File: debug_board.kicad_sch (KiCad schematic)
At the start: 0 parts

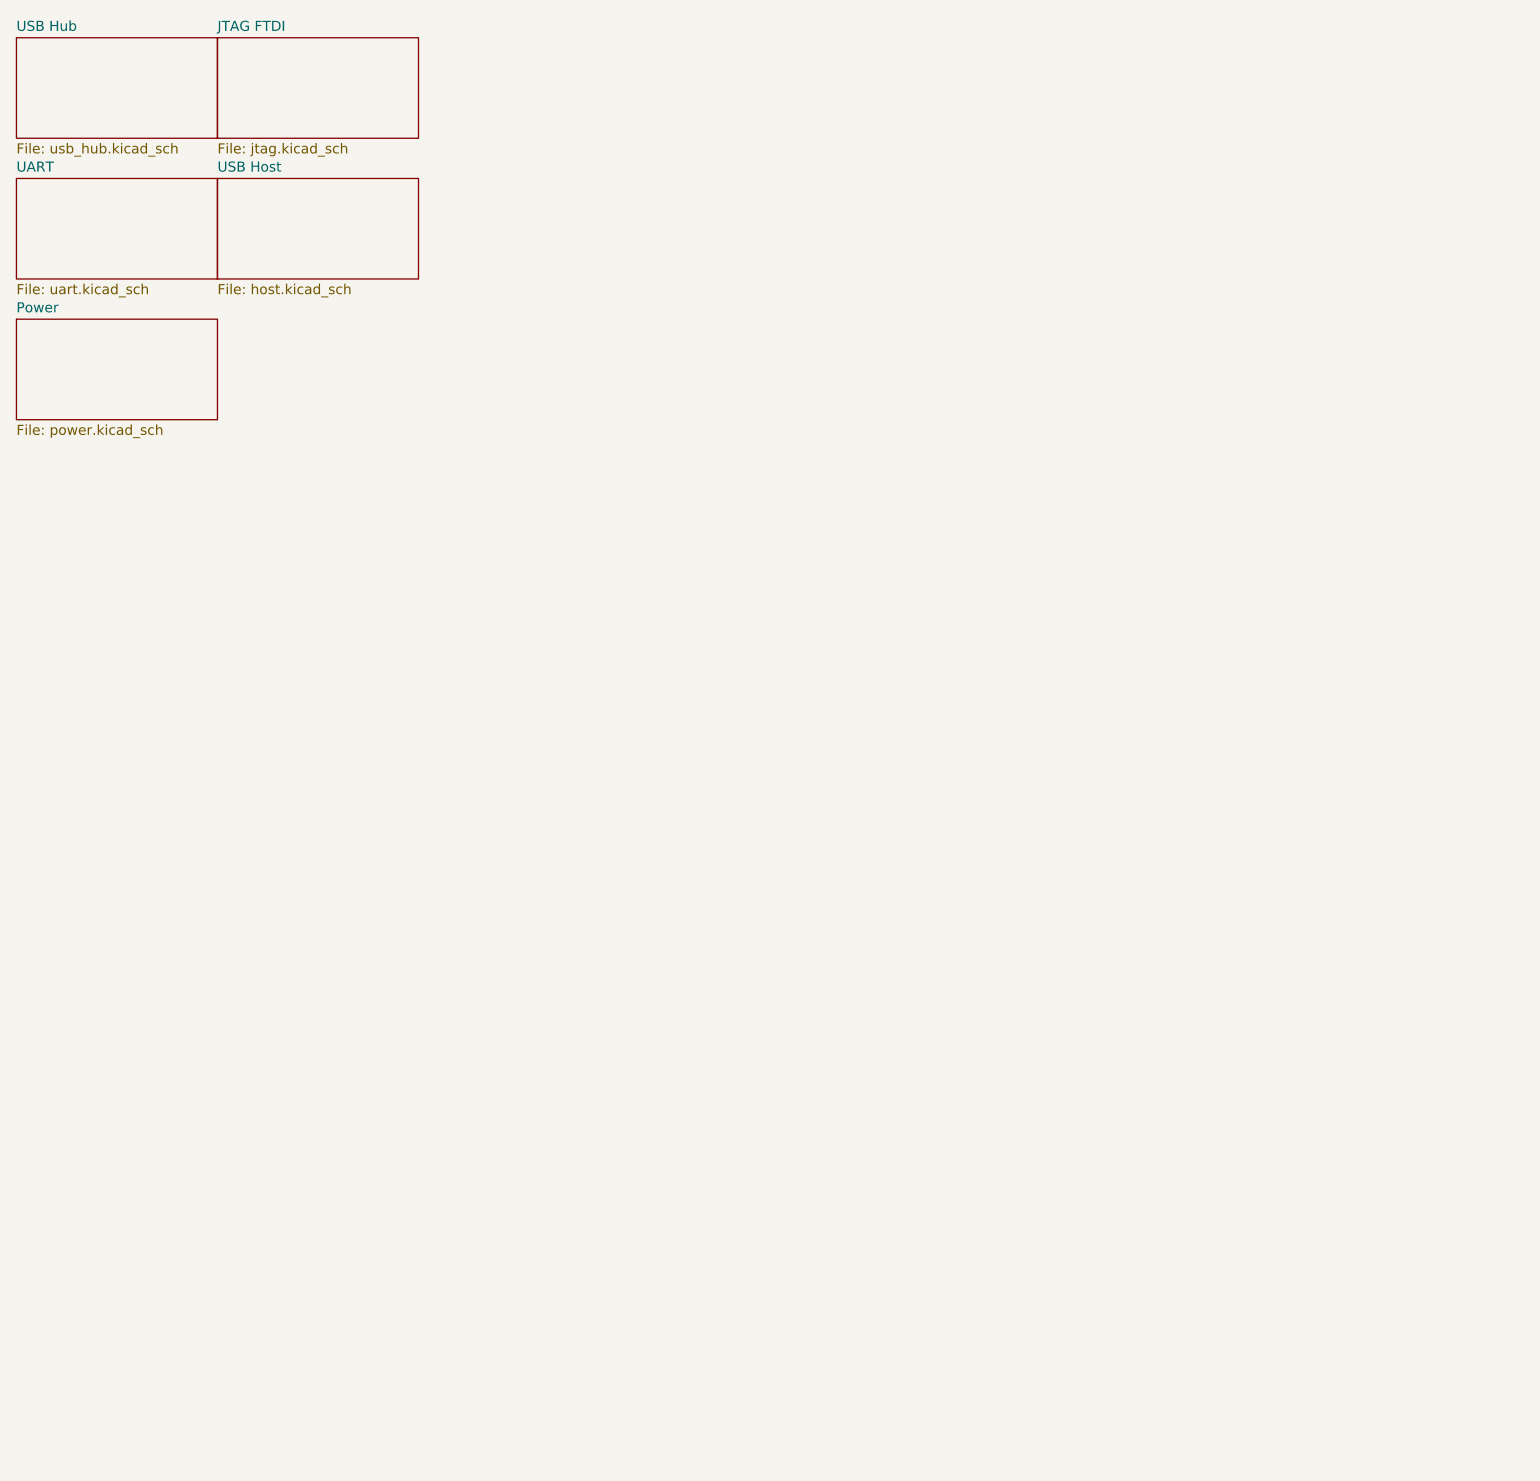
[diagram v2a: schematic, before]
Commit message: Used steppenprobe as base for our UART and JTAG.
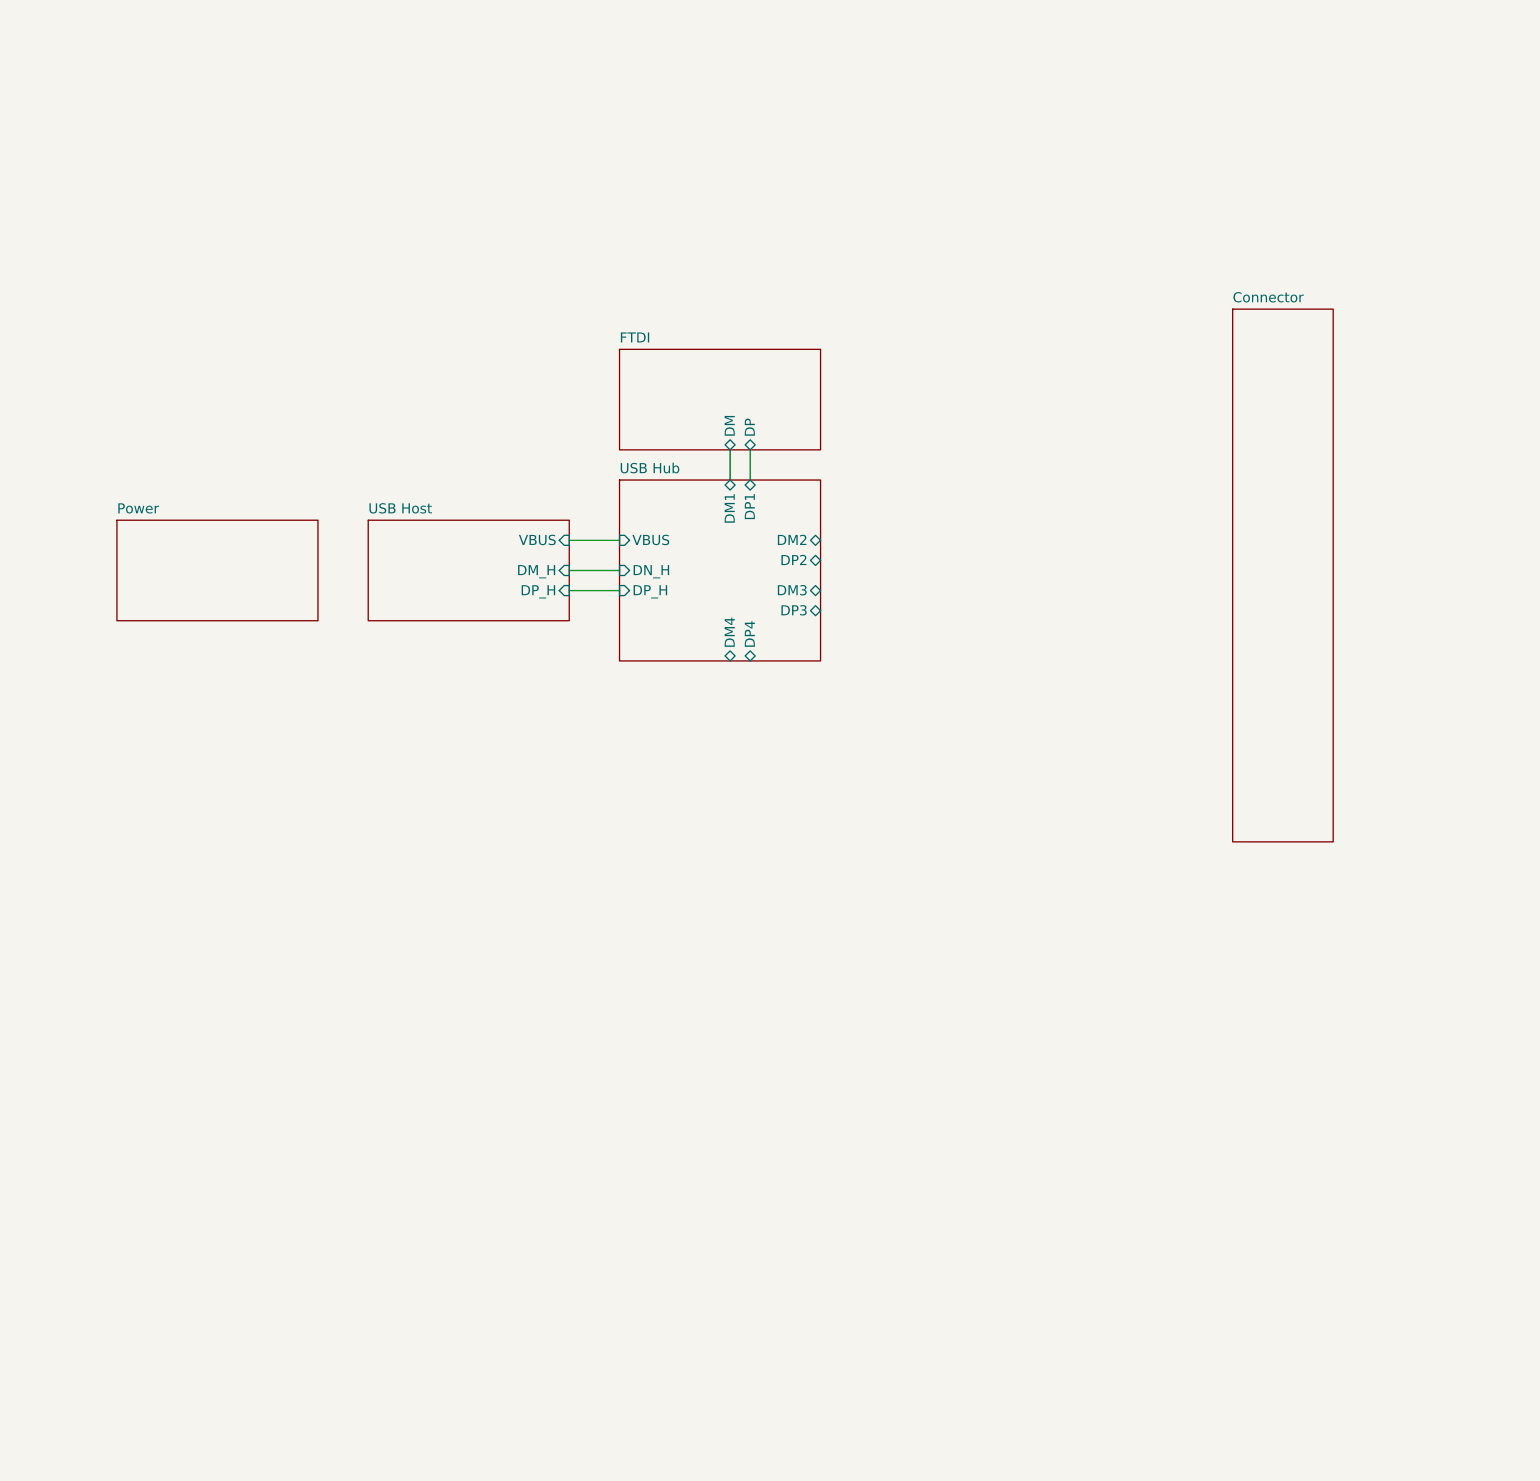
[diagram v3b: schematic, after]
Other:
- sheet JTAG FTDI renamed FTDI
- removed sheet UART
- added sheet Connector (connector.kicad_sch)
- sheet FTDI ports: added DM, DP; removed none
- sheet USB Host ports: added DM_H, DP_H, VBUS; removed none
- sheet USB Hub ports: added DM1, DM2, DM3, DM4, DN_H, DP1, DP2, DP3, DP4, DP_H, VBUS; removed none
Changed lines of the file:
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@@
 	(generator_version "8.0")
 	(paper "A4")
-	(sheet
-		(at 38.1 33.02)
+	(wire
+		(pts
+			(xy 82.55 82.55) (xy 88.9 82.55)
+		)
+		(stroke
+			(width 0)
+			(type default)
+		)
+	)
+	(wire
+		(pts
+			(xy 102.87 67.31) (xy 102.87 71.12)
+		)
+		(stroke
+			(width 0)
+			(type default)
+		)
+	)
+	(wire
+		(pts
+			(xy 105.41 67.31) (xy 105.41 71.12)
+		)
+		(stroke
+			(width 0)
+			(type default)
+		)
+	)
+	(wire
+		(pts
+			(xy 82.55 78.74) (xy 88.9 78.74)
+		)
+		(stroke
+			(width 0)
+			(type default)
+		)
+	)
+	(wire
+		(pts
+			(xy 82.55 85.09) (xy 88.9 85.09)
+		)
+		(stroke
+			(width 0)
+			(type default)
+		)
+	)
+	(sheet
+		(at 57.15 76.2)
 		(size 25.4 12.7)
 		(fields_autoplaced yes)
@@
 		)
 		(property "Sheetname" "USB Host"
-			(at 38.1 32.3084 0)
+			(at 57.15 75.4884 0)
 			(effects
 				(font
@@
 		)
 		(property "Sheetfile" "host.kicad_sch"
-			(at 38.1 46.3046 0)
-			(effects
-				(font
-					(size 1.27 1.27)
-				)
-				(justify left top)
+			(at 57.15 89.4846 0)
+			(effects
+				(font
+					(size 1.27 1.27)
+				)
+				(justify left top)
+				(hide yes)
+			)
+		)
+		(pin "VBUS" input
+			(at 82.55 78.74 0)
+			(effects
+				(font
+					(size 1.27 1.27)
+				)
+				(justify right)
+			)
+		)
+		(pin "DM_H" input
+			(at 82.55 82.55 0)
+			(effects
+				(font
+					(size 1.27 1.27)
+				)
+				(justify right)
+			)
+		)
+		(pin "DP_H" input
+			(at 82.55 85.09 0)
+			(effects
+				(font
+					(size 1.27 1.27)
+				)
+				(justify right)
 			)
 		)
@@
 	)
 	(sheet
-		(at 12.7 50.8)
+		(at 25.4 76.2)
 		(size 25.4 12.7)
 		(fields_autoplaced yes)
@@
 		)
 		(property "Sheetname" "Power"
-			(at 12.7 50.0884 0)
+			(at 25.4 75.4884 0)
 			(effects
 				(font
@@
 		)
 		(property "Sheetfile" "power.kicad_sch"
-			(at 12.7 64.0846 0)
-			(effects
-				(font
-					(size 1.27 1.27)
-				)
-				(justify left top)
+			(at 25.4 89.4846 0)
+			(effects
+				(font
+					(size 1.27 1.27)
+				)
+				(justify left top)
+				(hide yes)
 			)
 		)
@@
 	)
 	(sheet
-		(at 38.1 15.24)
+		(at 88.9 54.61)
 		(size 25.4 12.7)
 		(fields_autoplaced yes)
@@
 			(color 0 0 0 0.0000)
 		)
-		(property "Sheetname" "JTAG FTDI"
-			(at 38.1 14.5284 0)
+		(property "Sheetname" "FTDI"
+			(at 88.9 53.8984 0)
 			(effects
 				(font
@@
 		)
 		(property "Sheetfile" "jtag.kicad_sch"
-			(at 38.1 28.5246 0)
-			(effects
-				(font
-					(size 1.27 1.27)
-				)
-				(justify left top)
+			(at 88.9 67.8946 0)
+			(effects
+				(font
+					(size 1.27 1.27)
+				)
+				(justify left top)
+				(hide yes)
+			)
+		)
+		(pin "DM" bidirectional
+			(at 102.87 67.31 270)
+			(effects
+				(font
+					(size 1.27 1.27)
+				)
+				(justify left)
+			)
+		)
+		(pin "DP" bidirectional
+			(at 105.41 67.31 270)
+			(effects
+				(font
+					(size 1.27 1.27)
+				)
+				(justify left)
 			)
 		)
@@
 	)
 	(sheet
-		(at 12.7 33.02)
-		(size 25.4 12.7)
+		(at 88.9 71.12)
+		(size 25.4 22.86)
+		(stroke
+			(width 0.1524)
+			(type solid)
+		)
+		(fill
+			(color 0 0 0 0.0000)
+		)
+		(property "Sheetname" "USB Hub"
+			(at 88.9 70.4084 0)
+			(effects
+				(font
+					(size 1.27 1.27)
+				)
+				(justify left bottom)
+			)
+		)
+		(property "Sheetfile" "usb_hub.kicad_sch"
+			(at 98.044 69.088 0)
+			(effects
+				(font
+					(size 1.27 1.27)
+				)
+				(justify left top)
+				(hide yes)
+			)
+		)
+		(pin "DM2" bidirectional
+			(at 114.3 78.74 0)
+			(effects
+				(font
+					(size 1.27 1.27)
+				)
+				(justify right)
+			)
+		)
+		(pin "DM1" bidirectional
+			(at 102.87 71.12 90)
+			(effects
+				(font
+					(size 1.27 1.27)
+				)
+				(justify right)
+			)
+		)
+		(pin "DP1" bidirectional
+			(at 105.41 71.12 90)
+			(effects
+				(font
+					(size 1.27 1.27)
+				)
+				(justify right)
+			)
+		)
+		(pin "DP2" bidirectional
+			(at 114.3 81.28 0)
+			(effects
+				(font
+					(size 1.27 1.27)
+				)
+				(justify right)
+			)
+		)
+		(pin "DP3" bidirectional
+			(at 114.3 87.63 0)
+			(effects
+				(font
+					(size 1.27 1.27)
+				)
+				(justify right)
+			)
+		)
+		(pin "DM4" bidirectional
+			(at 102.87 93.98 270)
+			(effects
+				(font
+					(size 1.27 1.27)
+				)
+				(justify left)
+			)
+		)
+		(pin "DM3" bidirectional
+			(at 114.3 85.09 0)
+			(effects
+				(font
+					(size 1.27 1.27)
+				)
+				(justify right)
+			)
+		)
+		(pin "DP4" bidirectional
+			(at 105.41 93.98 270)
+			(effects
+				(font
+					(size 1.27 1.27)
+				)
+				(justify left)
+			)
+		)
+		(pin "VBUS" input
+			(at 88.9 78.74 180)
+			(effects
+				(font
+					(size 1.27 1.27)
+				)
+				(justify left)
+			)
+		)
+		(pin "DP_H" input
+			(at 88.9 85.09 180)
+			(effects
+				(font
+					(size 1.27 1.27)
+				)
+				(justify left)
+			)
+		)
+		(pin "DN_H" input
+			(at 88.9 82.55 180)
+			(effects
+				(font
+					(size 1.27 1.27)
+				)
+				(justify left)
+			)
+		)
+		(instances
+			(project "debug_board"
+				(path "/9ba02813-5189-4482-9c9e-35a29bc7aded"
+					(page "3")
+				)
+			)
+		)
+	)
+	(sheet
+		(at 166.37 49.53)
+		(size 12.7 67.31)
 		(fields_autoplaced yes)
 		(stroke
@@
 			(color 0 0 0 0.0000)
 		)
-		(property "Sheetname" "UART"
-			(at 12.7 32.3084 0)
-			(effects
-				(font
-					(size 1.27 1.27)
-				)
-				(justify left bottom)
-			)
-		)
-		(property "Sheetfile" "uart.kicad_sch"
-			(at 12.7 46.3046 0)
-			(effects
-				(font
-					(size 1.27 1.27)
-				)
-				(justify left top)
-			)
-		)
-		(instances
-			(project "debug_board"
-				(path "/9ba02813-5189-4482-9c9e-35a29bc7aded"
-					(page "5")
-				)
-			)
-		)
-	)
-	(sheet
-		(at 12.7 15.24)
-		(size 25.4 12.7)
-		(fields_autoplaced yes)
-		(stroke
-			(width 0.1524)
-			(type solid)
-		)
-		(fill
-			(color 0 0 0 0.0000)
-		)
-		(property "Sheetname" "USB Hub"
-			(at 12.7 14.5284 0)
-			(effects
-				(font
-					(size 1.27 1.27)
-				)
-				(justify left bottom)
-			)
-		)
-		(property "Sheetfile" "usb_hub.kicad_sch"
-			(at 12.7 28.5246 0)
-			(effects
-				(font
-					(size 1.27 1.27)
-				)
-				(justify left top)
-			)
-		)
-		(instances
-			(project "debug_board"
-				(path "/9ba02813-5189-4482-9c9e-35a29bc7aded"
-					(page "3")
-				)
-			)
+		(property "Sheetname" "Connector"
+			(at 166.37 48.8184 0)
+			(effects
+				(font
+					(size 1.27 1.27)
+				)
+				(justify left bottom)
+			)
+		)
+		(property "Sheetfile" "connector.kicad_sch"
+			(at 166.37 117.4246 0)
+			(effects
+				(font
+					(size 1.27 1.27)
+				)
+				(justify left top)
+				(hide yes)
+			)
+		)
+		(instances
+			(project "debug_board"
+				(path "/9ba02813-5189-4482-9c9e-35a29bc7aded"
+					(page "7")
+				)
+			)

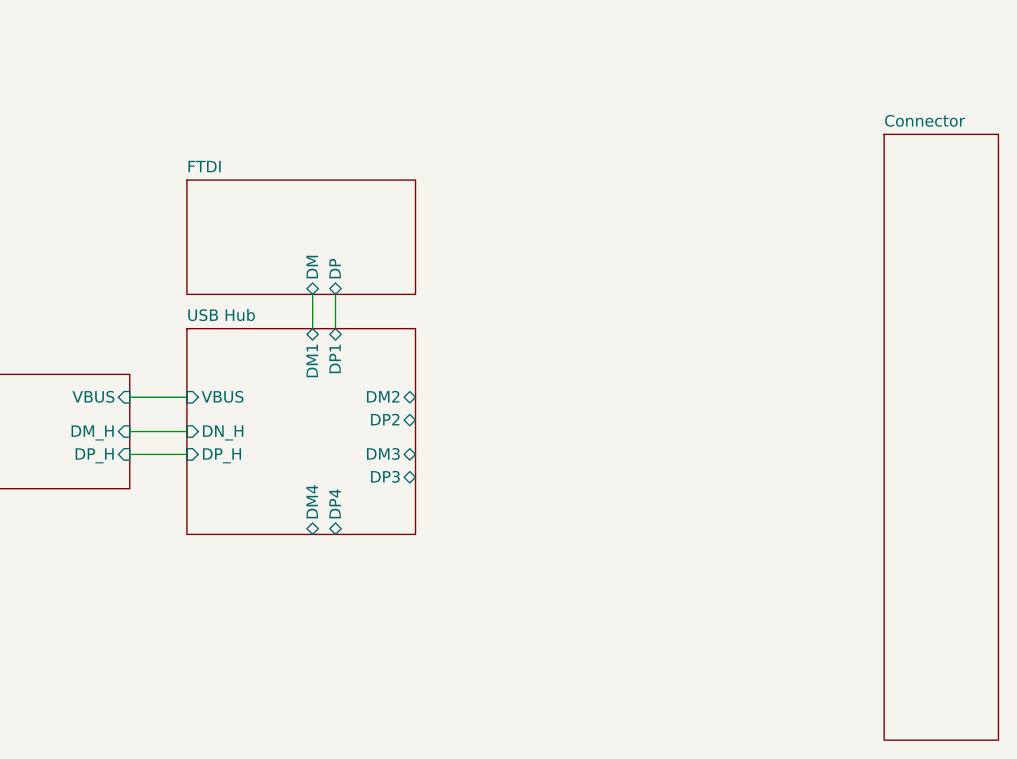
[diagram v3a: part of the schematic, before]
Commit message: updated edge connector
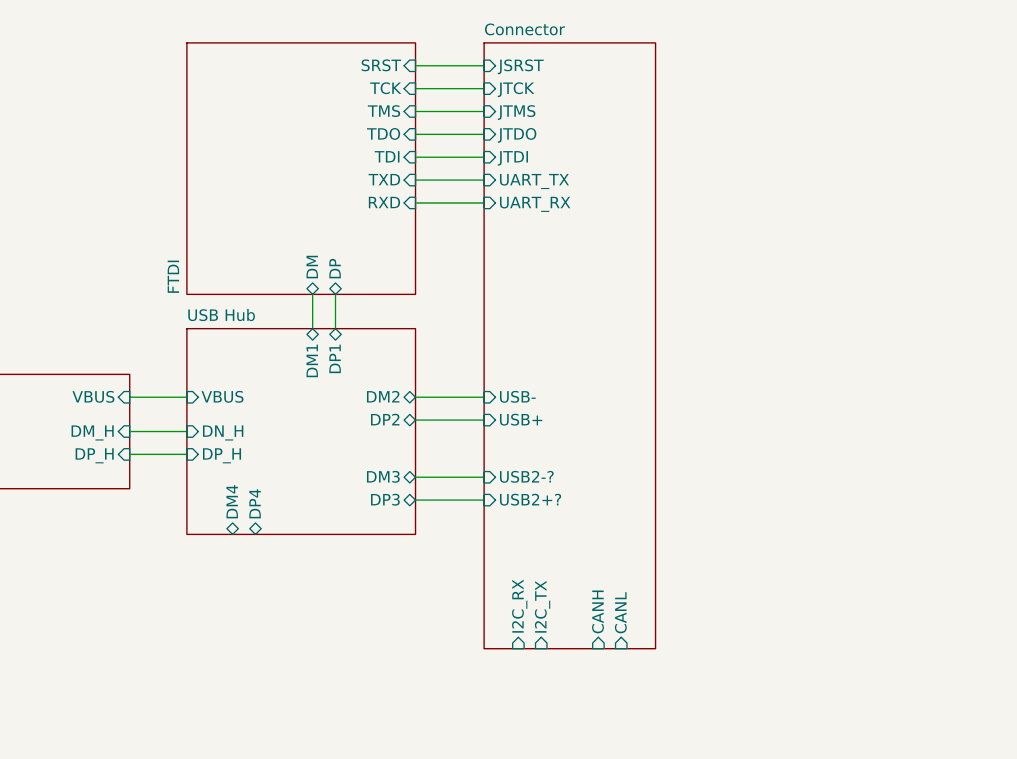
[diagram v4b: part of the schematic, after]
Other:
- sheet Connector ports: added CANH, CANL, I2C_RX, I2C_TX, JSRST, JTCK, JTDI, JTDO, JTMS, UART_RX, UART_TX, USB+, USB-, USB2+?, USB2-?; removed none
- sheet FTDI ports: added RXD, SRST, TCK, TDI, TDO, TMS, TXD; removed none

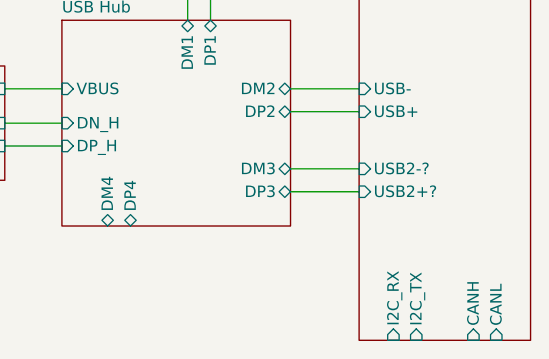
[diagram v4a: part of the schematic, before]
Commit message: renamed i2c
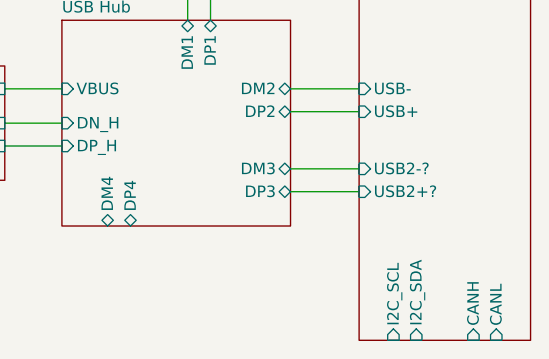
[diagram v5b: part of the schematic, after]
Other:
- sheet Connector ports: added I2C_SCL, I2C_SDA; removed I2C_RX, I2C_TX
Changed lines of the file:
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@@
-			)
-		)
-		(pin "I2C_TX" input
-			(at 128.27 106.68 270)
-			(effects
-				(font
-					(size 1.27 1.27)
-				)
-				(justify left)
-			)
-		)
-		(pin "I2C_RX" input
-			(at 125.73 106.68 270)
-			(effects
-				(font
-					(size 1.27 1.27)
-				)
-				(justify left)
 			)
 		)
@@
 			(effects
 				(font
+					(size 1.27 1.27)
+				)
+				(justify left)
+			)
+		)
+		(pin "I2C_SCL" input
+			(at 125.73 106.68 270)
+			(effects
+				(font
+					(size 1.27 1.27)
+				)
+				(justify left)
+			)
+		)
+		(pin "I2C_SDA" input
+			(at 128.27 106.68 270)
+			(effects
+				(font

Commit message: STM32 schematic
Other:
- added sheet STM32 (STM32.kicad_sch)
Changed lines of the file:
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@@
+	)
+	(sheet
+		(at 60.96 50.8)
+		(size 21.59 11.43)
+		(fields_autoplaced yes)
+		(stroke
+			(width 0.1524)
+			(type solid)
+		)
+		(fill
+			(color 0 0 0 0.0000)
+		)
+		(property "Sheetname" "STM32"
+			(at 60.96 50.0884 0)
+			(effects
+				(font
+					(size 1.27 1.27)
+				)
+				(justify left bottom)
+			)
+		)
+		(property "Sheetfile" "STM32.kicad_sch"
+			(at 60.96 62.8146 0)
+			(effects
+				(font
+					(size 1.27 1.27)
+				)
+				(justify left top)
+			)
+		)
+		(instances
+			(project "debug_board"
+				(path "/9ba02813-5189-4482-9c9e-35a29bc7aded"
+					(page "8")
+				)
+			)
+		)
 	)
 	(sheet
